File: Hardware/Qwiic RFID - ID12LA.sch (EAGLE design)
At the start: 29 parts, among them J2 SMD, J3 PTH, J4 SMD, J8 AVR_SPI_PROG_3X2TESTPOINTS, U1 ATTINY84

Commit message: Schematic organization
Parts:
- removed J7: (no value), SparkFun-Connectors:CONN_01PTH_NO_SILK_YES_STOP
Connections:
- net CP: now also U1.(ADC7)PA7; no longer J7.1
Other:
- note added: "Elias Santistevan"
- moved on the sheet: D1, J8, JP7, JP8, R1, R2, R3, U1

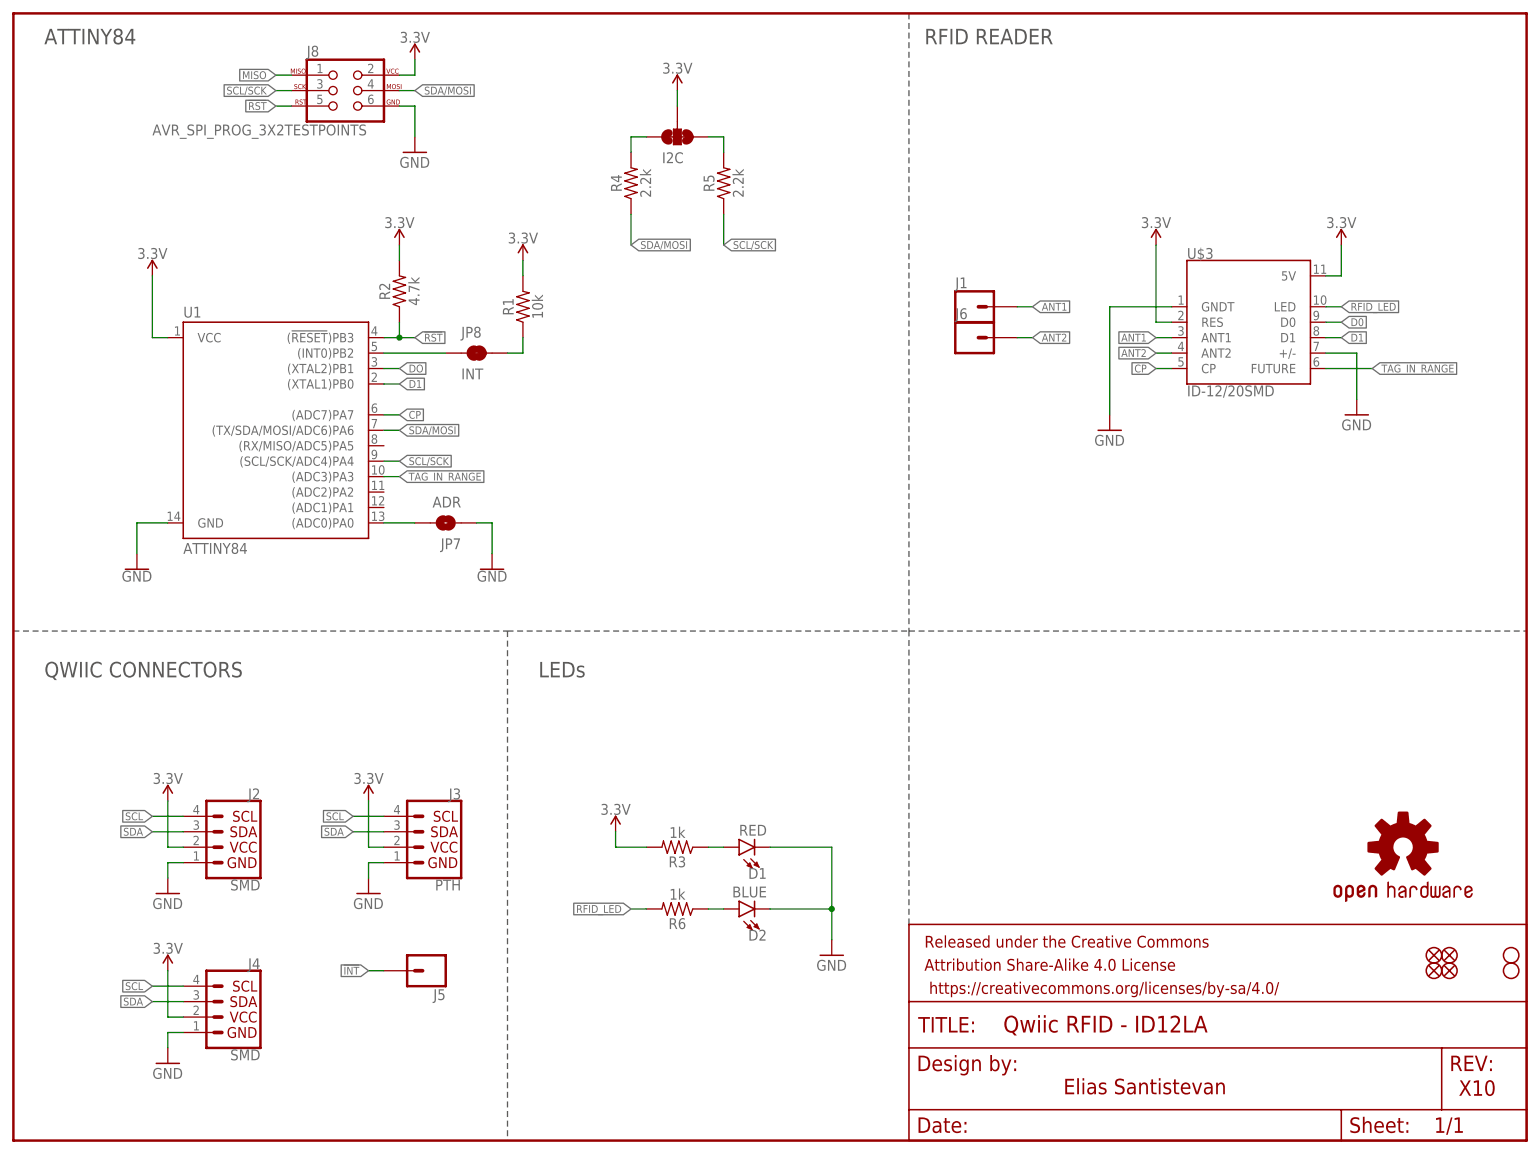
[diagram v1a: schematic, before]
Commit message: Moved to double sided to decrease size of product
Buzzer, LED, and RFID connector live on top.
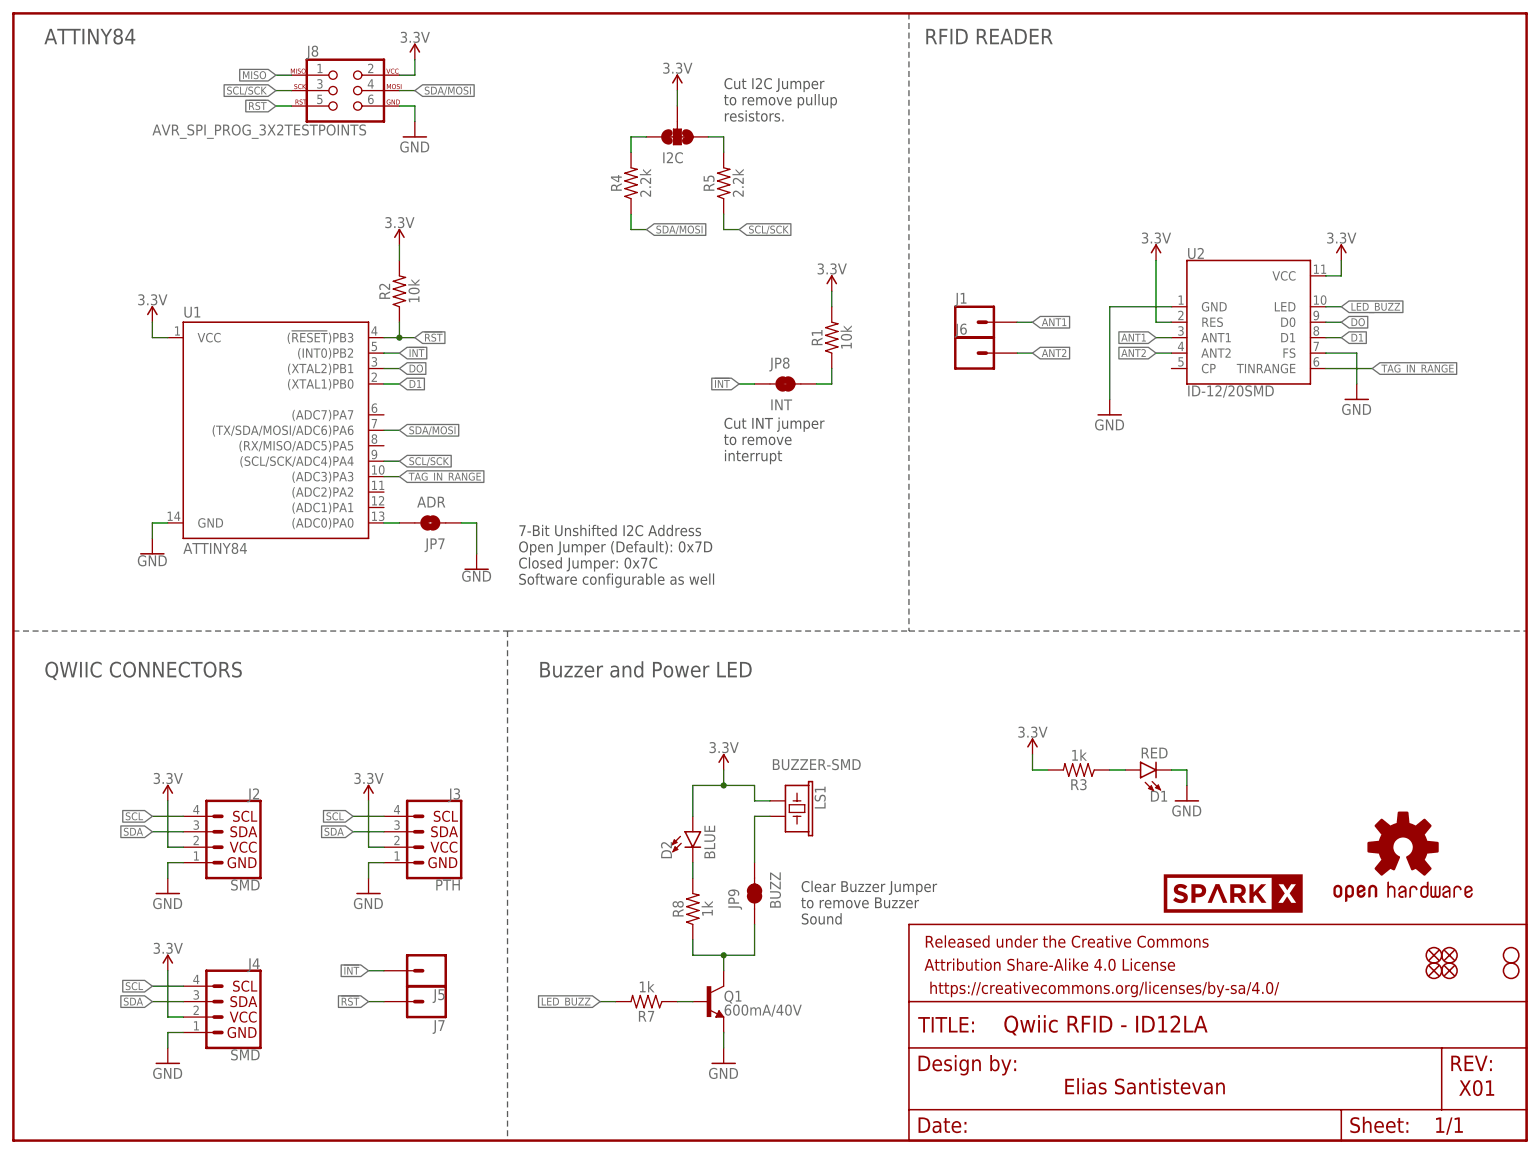
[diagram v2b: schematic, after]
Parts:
- removed R6: 1k, SparkFun-Resistors:1KOHM-0603-1/10W-1%
- added J7: (no value), SparkFun-Connectors:CONN_01PTH_NO_SILK_YES_STOP
- added JP9: BUZZ, SparkFun-Jumpers:JUMPER-SMT_2_NC_TRACE_SILK
- added LS1: BUZZER-SMD, SparkFun-Electromechanical:BUZZER-SMD
- added Q1: 600mA/40V, SparkFun-DiscreteSemi:TRANS_NPN-MMBT2222AL
- added R7, R8: 1k, SparkFun-Resistors:1KOHM-0603-1/10W-1%
- added U$4: SPARKX-LOGO3, SparkX:SPARKX-LOGO3
- R2: value 4.7k -> 10k; device SparkFun-Resistors:4.7KOHM-0603-1/10W-1% -> SparkFun-Resistors:10KOHM-0603-1/10W-1%
- renumbered U$3 to U2
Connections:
- removed net CP: U1.(ADC7)PA7, U2.CP
- removed net D0: U2.D0
- removed net N$11: D2.A, R6.1
- removed net RFID_LED: R6.2, U2.LED
- new net LED_BUZZ: R7.2, U2.LED
- new net N$5: D2.C, R8.2
- new net N$8: JP9.1, Q1.C, R8.1
- new net N$9: JP9.2, LS1.2
- net !INT: now also JP8.1, U1.(INT0)PB2
- net !RST: now also J7.1
- net 3.3V: now also D2.A, LS1.1, U2.VCC; no longer U2.5V
- net DO: now also U2.D0
- net GND: now also Q1.E, U2.FS, U2.GND; no longer D2.C, U2.+/-, U2.GNDT
- net N$7: now also Q1.B, R7.1; no longer JP8.1, U1.(INT0)PB2
- net TAG_IN_RANGE: now also U2.TINRANGE; no longer U2.FUTURE
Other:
- note added: "7-Bit Unshifted I2C Address Open Jumper (Default): 0x7D Closed Jumper: 0x7C Software configurable as well"
- note added: "Buzzer and Power LED"
- note added: "Clear Buzzer Jumper to remove Buzzer Sound"
- note added: "Cut I2C Jumper to remove pullup resistors."
- note added: "Cut INT jumper to remove interrupt"
- note added: "X01"
- note removed: "LEDs"
- note removed: "X10"
- moved on the sheet: D1, D2, J1, J6, JP7, JP8, R1, R3
